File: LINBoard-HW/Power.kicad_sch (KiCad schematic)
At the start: 18 parts, among them U3 TPS56339DDC, U4 LD1117S33CTR

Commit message: board layout started
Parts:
- C24, C25, C26, C27, C28, C29, C30, C31: footprint Capacitor_SMD:C_0603_1608Metric -> Capacitor_SMD:C_0402_1005Metric
- D3: value SCHOTTKY -> Schottky; footprint (none) -> Diode_SMD:D_SOD-123
- D6: footprint LED_SMD:LED_0805_2012Metric -> LED_SMD:LED_0603_1608Metric
- L2: footprint (none) -> Inductors_SMD:Wuerth_LHMI
- R21, R22, R23, R24: footprint Resistor_SMD:R_0603_1608Metric -> Resistor_SMD:R_0402_1005Metric
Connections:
- net SW: now reaches C27.2, L2.1, U3.2 (SW)
- net +12P: now reaches C24.1, C25.1, C26.1, D3.1 (K), U3.3 (VIN)
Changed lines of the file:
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@@
+	)
+	(junction
+		(at 35.56 31.75)
+		(diameter 0)
+		(color 0 0 0 0)
 	)
 	(junction
@@
 	(wire
 		(pts
+			(xy 35.56 29.21) (xy 35.56 31.75)
+		)
+		(stroke
+			(width 0)
+			(type default)
+		)
+	)
+	(wire
+		(pts
 			(xy 200.66 45.72) (xy 200.66 48.26)
 		)
@@
 			(width 0)
 			(type default)
+		)
+	)
+	(label "SW"
+		(at 96.52 34.29 0)
+		(effects
+			(font
+				(size 1.27 1.27)
+				(thickness 0.254)
+				(bold yes)
+			)
+			(justify left bottom)
 		)
 	)
@@
 			)
 		)
-		(property "Footprint" "Resistor_SMD:R_0603_1608Metric"
+		(property "Footprint" "Resistor_SMD:R_0402_1005Metric"
 			(at 200.66 43.18 0)
 			(effects
@@
 			)
 		)
-		(property "Footprint" "Resistor_SMD:R_0603_1608Metric"
+		(property "Footprint" "Resistor_SMD:R_0402_1005Metric"
 			(at 95.25 43.18 0)
 			(effects
@@
 			)
 		)
-		(property "Footprint" ""
+		(property "Footprint" "Inductors_SMD:Wuerth_LHMI"
 			(at 113.03 34.29 0)
 			(effects
@@
 			)
 		)
-		(property "Footprint" "Capacitor_SMD:C_0603_1608Metric"
+		(property "Footprint" "Capacitor_SMD:C_0402_1005Metric"
 			(at 55.88 44.45 0)
 			(effects
@@
 			)
 		)
-		(property "Footprint" "Resistor_SMD:R_0603_1608Metric"
+		(property "Footprint" "Resistor_SMD:R_0402_1005Metric"
 			(at 119.38 44.45 0)
 			(effects
@@
 			)
 		)
-		(property "Footprint" "Capacitor_SMD:C_0603_1608Metric"
+		(property "Footprint" "Capacitor_SMD:C_0402_1005Metric"
 			(at 101.6 43.18 0)
 			(effects
@@
 			)
 		)
-		(property "Footprint" "Capacitor_SMD:C_0603_1608Metric"
+		(property "Footprint" "Capacitor_SMD:C_0402_1005Metric"
 			(at 132.08 39.37 0)
 			(effects
@@
 			)
 		)
-		(property "Footprint" "Resistor_SMD:R_0603_1608Metric"
+		(property "Footprint" "Resistor_SMD:R_0402_1005Metric"
 			(at 119.38 54.61 0)
 			(effects
@@
 			)
 		)
-		(property "Footprint" "Capacitor_SMD:C_0603_1608Metric"
+		(property "Footprint" "Capacitor_SMD:C_0402_1005Metric"
 			(at 35.56 44.45 0)
 			(effects
@@
 			)
 		)
-		(property "Footprint" "Capacitor_SMD:C_0603_1608Metric"
+		(property "Footprint" "Capacitor_SMD:C_0402_1005Metric"
 			(at 187.96 39.37 0)
 			(effects
@@
 			)
 		)
-		(property "Footprint" "LED_SMD:LED_0805_2012Metric"
+		(property "Footprint" "LED_SMD:LED_0603_1608Metric"
 			(at 200.66 50.8 90)
 			(effects
@@
 			)
 		)
-		(property "Footprint" "Capacitor_SMD:C_0603_1608Metric"
+		(property "Footprint" "Capacitor_SMD:C_0402_1005Metric"
 			(at 45.72 44.45 0)
 			(effects
@@
 			)
 		)
-		(property "Footprint" "Capacitor_SMD:C_0603_1608Metric"
+		(property "Footprint" "Capacitor_SMD:C_0402_1005Metric"
 			(at 157.48 39.37 0)
 			(effects
@@
 	)
 	(symbol
+		(lib_id "power:+12P")
+		(at 35.56 29.21 0)
+		(unit 1)
+		(exclude_from_sim no)
+		(in_bom yes)
+		(on_board yes)
+		(dnp no)
+		(fields_autoplaced yes)
+		(property "Reference" "#PWR045"
+			(at 35.56 33.02 0)
+			(effects
+				(font
+					(size 1.27 1.27)
+				)
+				(hide yes)
+			)
+		)
+		(property "Value" "+12P"
+			(at 35.56 24.13 0)
+			(effects
+				(font
+					(size 1.27 1.27)
+				)
+			)
+		)
+		(property "Footprint" ""
+			(at 35.56 29.21 0)
+			(effects
+				(font
+					(size 1.27 1.27)
+				)
+				(hide yes)
+			)
+		)
+		(property "Datasheet" ""
+			(at 35.56 29.21 0)
+			(effects
+				(font
+					(size 1.27 1.27)
+				)
+				(hide yes)
+			)
+		)
+		(property "Description" "Power symbol creates a global label with name \"+12P\""
+			(at 35.56 29.21 0)
+			(effects
+				(font
+					(size 1.27 1.27)
+				)
+				(hide yes)
+			)
+		)
+		(pin "1"
+		)
+		(instances
+			(project ""
+				(path "/27863e5d-8a22-474c-850d-36d8970b0f4a/f2430bd2-0c34-49e2-a275-9ffcb384aba8"
+					(reference "#PWR045")
+					(unit 1)
+				)
+			)
+		)
+	)
+	(symbol
 		(lib_id "Jumper:Jumper_2_Small_Bridged")
 		(at 200.66 38.1 90)
@@
 			)
 		)
-		(property "Footprint" "Capacitor_SMD:C_0603_1608Metric"
+		(property "Footprint" "Capacitor_SMD:C_0402_1005Metric"
 			(at 142.24 39.37 0)
 			(effects
@@
 			)
 		)
-		(property "Value" "SCHOTTKY"
+		(property "Value" "Schottky"
 			(at 28.194 37.592 0)
 			(effects
@@
 			)
 		)
-		(property "Footprint" ""
+		(property "Footprint" "Diode_SMD:D_SOD-123"
 			(at 27.94 31.75 90)
 			(effects

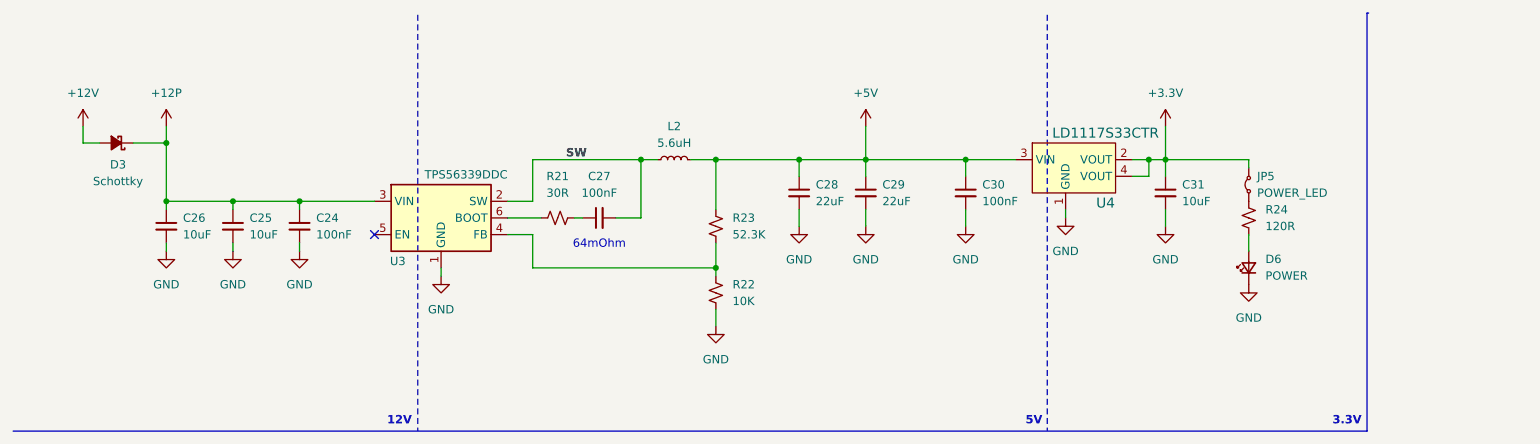
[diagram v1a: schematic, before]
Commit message: change usb
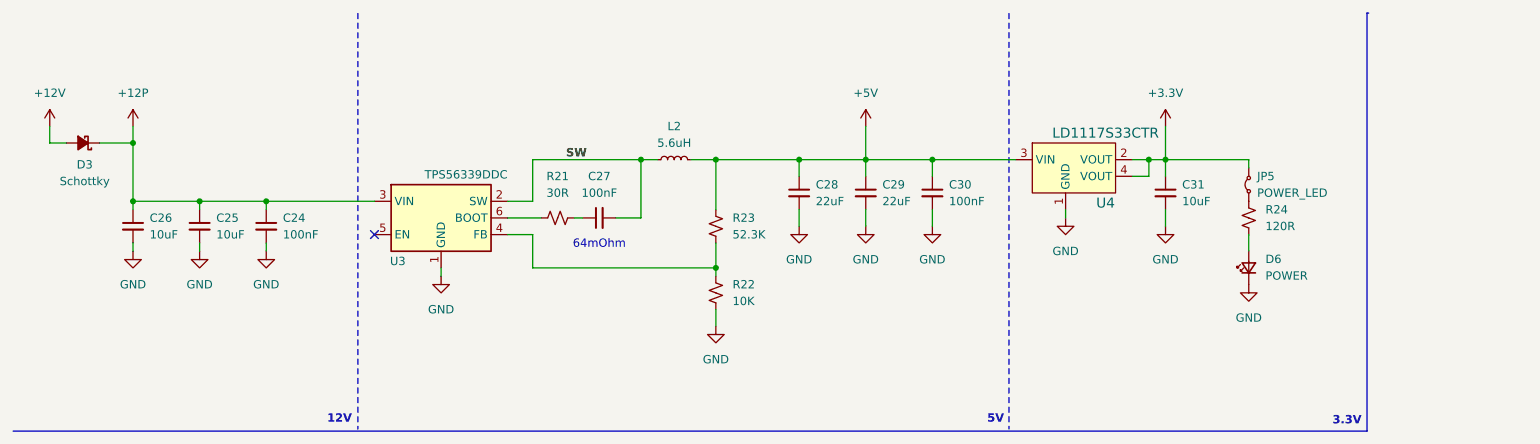
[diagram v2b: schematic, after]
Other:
- moved on the sheet: C24, C25, C26, C30, D3

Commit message: doing some layout
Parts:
- C24, C25, C26, C27, C28, C29, C30, C31: footprint Capacitor_SMD:C_0402_1005Metric -> Capacitor_SMD:C_0805_2012Metric
- D6: footprint LED_SMD:LED_0603_1608Metric -> LED_SMD:LED_0805_2012Metric
- R21, R22, R23, R24: footprint Resistor_SMD:R_0402_1005Metric -> Resistor_SMD:R_0805_2012Metric
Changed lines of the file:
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@@
 			)
 		)
-		(property "Footprint" "Resistor_SMD:R_0402_1005Metric"
+		(property "Footprint" "Resistor_SMD:R_0805_2012Metric"
 			(at 200.66 43.18 0)
 			(effects
@@
 			)
 		)
-		(property "Footprint" "Resistor_SMD:R_0402_1005Metric"
+		(property "Footprint" "Resistor_SMD:R_0805_2012Metric"
 			(at 95.25 43.18 0)
 			(effects
@@
 			)
 		)
-		(property "Footprint" "Capacitor_SMD:C_0402_1005Metric"
+		(property "Footprint" "Capacitor_SMD:C_0805_2012Metric"
 			(at 50.8 44.45 0)
 			(effects
@@
 			)
 		)
-		(property "Footprint" "Resistor_SMD:R_0402_1005Metric"
+		(property "Footprint" "Resistor_SMD:R_0805_2012Metric"
 			(at 119.38 44.45 0)
 			(effects
@@
 			)
 		)
-		(property "Footprint" "Capacitor_SMD:C_0402_1005Metric"
+		(property "Footprint" "Capacitor_SMD:C_0805_2012Metric"
 			(at 101.6 43.18 0)
 			(effects
@@
 			)
 		)
-		(property "Footprint" "Capacitor_SMD:C_0402_1005Metric"
+		(property "Footprint" "Capacitor_SMD:C_0805_2012Metric"
 			(at 132.08 39.37 0)
 			(effects
@@
 			)
 		)
-		(property "Footprint" "Resistor_SMD:R_0402_1005Metric"
+		(property "Footprint" "Resistor_SMD:R_0805_2012Metric"
 			(at 119.38 54.61 0)
 			(effects
@@
 			)
 		)
-		(property "Footprint" "Capacitor_SMD:C_0402_1005Metric"
+		(property "Footprint" "Capacitor_SMD:C_0805_2012Metric"
 			(at 30.48 44.45 0)
 			(effects
@@
 			)
 		)
-		(property "Footprint" "Capacitor_SMD:C_0402_1005Metric"
+		(property "Footprint" "Capacitor_SMD:C_0805_2012Metric"
 			(at 187.96 39.37 0)
 			(effects
@@
 			)
 		)
-		(property "Footprint" "LED_SMD:LED_0603_1608Metric"
+		(property "Footprint" "LED_SMD:LED_0805_2012Metric"
 			(at 200.66 50.8 90)
 			(effects
@@
 			)
 		)
-		(property "Footprint" "Capacitor_SMD:C_0402_1005Metric"
+		(property "Footprint" "Capacitor_SMD:C_0805_2012Metric"
 			(at 40.64 44.45 0)
 			(effects
@@
 			)
 		)
-		(property "Footprint" "Capacitor_SMD:C_0402_1005Metric"
+		(property "Footprint" "Capacitor_SMD:C_0805_2012Metric"
 			(at 152.4 39.37 0)
 			(effects
@@
 			)
 		)
-		(property "Footprint" "Capacitor_SMD:C_0402_1005Metric"
+		(property "Footprint" "Capacitor_SMD:C_0805_2012Metric"
 			(at 142.24 39.37 0)
 			(effects

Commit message: routing first pass complete
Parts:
- removed D3: Schottky, Diode_SMD:D_SOD-123, symbol Device:D_Schottky_Small_Filled
- added D9: Schottky, Diode_SMD:D_SOD-123, symbol Device:D_Schottky_Small_Filled
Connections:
- net +12P: now also D9.1 (K)
- net +12V: now also D9.2 (A)
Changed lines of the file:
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@@
+	)
+	(junction
+		(at 30.48 22.86)
+		(diameter 0)
+		(color 0 0 0 0)
 	)
 	(junction
@@
 	)
 	(junction
-		(at 30.48 31.75)
-		(diameter 0)
-		(color 0 0 0 0)
-	)
-	(junction
 		(at 50.8 40.64)
 		(diameter 0)
@@
 	(wire
 		(pts
-			(xy 30.48 29.21) (xy 30.48 31.75)
+			(xy 30.48 20.32) (xy 30.48 22.86)
 		)
 		(stroke
@@
 	(wire
 		(pts
-			(xy 25.4 31.75) (xy 30.48 31.75)
-		)
-		(stroke
-			(width 0)
-			(type default)
-		)
-	)
-	(wire
-		(pts
 			(xy 50.8 48.26) (xy 50.8 46.99)
 		)
@@
 	(wire
 		(pts
-			(xy 17.78 29.21) (xy 17.78 31.75)
-		)
-		(stroke
-			(width 0)
-			(type default)
-		)
-	)
-	(wire
-		(pts
-			(xy 17.78 31.75) (xy 20.32 31.75)
+			(xy 17.78 20.32) (xy 17.78 22.86)
 		)
 		(stroke
@@
 	(wire
 		(pts
-			(xy 30.48 31.75) (xy 30.48 40.64)
-		)
-		(stroke
-			(width 0)
-			(type default)
-		)
-	)
-	(wire
-		(pts
 			(xy 119.38 57.15) (xy 119.38 59.69)
 		)
@@
 	(wire
 		(pts
+			(xy 17.78 22.86) (xy 20.32 22.86)
+		)
+		(stroke
+			(width 0)
+			(type default)
+		)
+	)
+	(wire
+		(pts
 			(xy 91.44 40.64) (xy 91.44 34.29)
 		)
@@
 	(wire
 		(pts
+			(xy 30.48 22.86) (xy 30.48 40.64)
+		)
+		(stroke
+			(width 0)
+			(type default)
+		)
+	)
+	(wire
+		(pts
 			(xy 185.42 36.83) (xy 185.42 34.29)
 		)
@@
 		(pts
 			(xy 152.4 34.29) (xy 152.4 36.83)
+		)
+		(stroke
+			(width 0)
+			(type default)
+		)
+	)
+	(wire
+		(pts
+			(xy 25.4 22.86) (xy 30.48 22.86)
 		)
 		(stroke
@@
 	)
 	(symbol
+		(lib_id "Device:D_Schottky_Small_Filled")
+		(at 22.86 22.86 180)
+		(unit 1)
+		(exclude_from_sim no)
+		(in_bom yes)
+		(on_board yes)
+		(dnp no)
+		(property "Reference" "D9"
+			(at 23.114 26.162 0)
+			(effects
+				(font
+					(size 1.27 1.27)
+				)
+			)
+		)
+		(property "Value" "Schottky"
+			(at 23.114 28.702 0)
+			(effects
+				(font
+					(size 1.27 1.27)
+				)
+			)
+		)
+		(property "Footprint" "Diode_SMD:D_SOD-123"
+			(at 22.86 22.86 90)
+			(effects
+				(font
+					(size 1.27 1.27)
+				)
+				(hide yes)
+			)
+		)
+		(property "Datasheet" "~"
+			(at 22.86 22.86 90)
+			(effects
+				(font
+					(size 1.27 1.27)
+				)
+				(hide yes)
+			)
+		)
+		(property "Description" "Schottky diode, small symbol, filled shape"
+			(at 22.86 22.86 0)
+			(effects
+				(font
+					(size 1.27 1.27)
+				)
+				(hide yes)
+			)
+		)
+		(pin "1"
+		)
+		(pin "2"
+		)
+		(instances
+			(project "LINBoard-HW"
+				(path "/27863e5d-8a22-474c-850d-36d8970b0f4a/f2430bd2-0c34-49e2-a275-9ffcb384aba8"
+					(reference "D9")
+					(unit 1)
+				)
+			)
+		)
+	)
+	(symbol
 		(lib_id "power:GND")
 		(at 187.96 44.45 0)
@@
 	(symbol
 		(lib_id "power:+12V")
-		(at 17.78 29.21 0)
+		(at 17.78 20.32 0)
 		(unit 1)
 		(exclude_from_sim no)
@@
 		(fields_autoplaced yes)
 		(property "Reference" "#PWR07"
-			(at 17.78 33.02 0)
+			(at 17.78 24.13 0)
 			(effects
 				(font
@@
 		)
 		(property "Value" "+12V"
-			(at 17.78 24.13 0)
+			(at 17.78 15.24 0)
 			(effects
 				(font
@@
 		)
 		(property "Footprint" ""
-			(at 17.78 29.21 0)
+			(at 17.78 20.32 0)
 			(effects
 				(font
@@
 		)
 		(property "Datasheet" ""
-			(at 17.78 29.21 0)
+			(at 17.78 20.32 0)
 			(effects
 				(font
@@
 		)
 		(property "Description" "Power symbol creates a global label with name \"+12V\""
-			(at 17.78 29.21 0)
+			(at 17.78 20.32 0)
 			(effects
 				(font
@@
 	(symbol
 		(lib_id "power:+12P")
-		(at 30.48 29.21 0)
+		(at 30.48 20.32 0)
 		(unit 1)
 		(exclude_from_sim no)
@@
 		(fields_autoplaced yes)
 		(property "Reference" "#PWR045"
-			(at 30.48 33.02 0)
+			(at 30.48 24.13 0)
 			(effects
 				(font
@@
 		)
 		(property "Value" "+12P"
-			(at 30.48 24.13 0)
+			(at 30.48 15.24 0)
 			(effects
 				(font
@@
 		)
 		(property "Footprint" ""
-			(at 30.48 29.21 0)
+			(at 30.48 20.32 0)
 			(effects
 				(font
@@
 		)
 		(property "Datasheet" ""
-			(at 30.48 29.21 0)
+			(at 30.48 20.32 0)
 			(effects
 				(font
@@
 		)
 		(property "Description" "Power symbol creates a global label with name \"+12P\""
-			(at 30.48 29.21 0)
+			(at 30.48 20.32 0)
 			(effects
 				(font
@@
 					(unit 1)
 				)
-			)
-		)
-	)
-	(symbol
-		(lib_id "Device:D_Schottky_Small_Filled")
-		(at 22.86 31.75 180)
-		(unit 1)
-		(exclude_from_sim no)
-		(in_bom yes)
-		(on_board yes)
-		(dnp no)
-		(property "Reference" "D3"
-			(at 23.114 35.052 0)
-			(effects
-				(font
-					(size 1.27 1.27)
-				)
-			)
-		)
-		(property "Value" "Schottky"
-			(at 23.114 37.592 0)
-			(effects
-				(font
-					(size 1.27 1.27)
-				)
-			)
-		)
-		(property "Footprint" "Diode_SMD:D_SOD-123"
-			(at 22.86 31.75 90)
-			(effects
-				(font
-					(size 1.27 1.27)
-				)
-				(hide yes)
-			)
-		)
-		(property "Datasheet" "~"
-			(at 22.86 31.75 90)
-			(effects
-				(font
-					(size 1.27 1.27)
-				)
-				(hide yes)
-			)
-		)
-		(property "Description" "Schottky diode, small symbol, filled shape"
-			(at 22.86 31.75 0)
-			(effects
-				(font
-					(size 1.27 1.27)
-				)
-				(hide yes)
-			)
-		)
-		(pin "1"
-		)
-		(pin "2"
-		)
-		(instances
-			(project "LINBoard-HW"
-				(path "/27863e5d-8a22-474c-850d-36d8970b0f4a/f2430bd2-0c34-49e2-a275-9ffcb384aba8"
-					(reference "D3")
-					(unit 1)
-				)

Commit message: add fab outputs
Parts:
- C24, C27, C30: LCSC Part (none) -> C49678
- C25, C26, C31: LCSC Part (none) -> C15850
- C28, C29: LCSC Part (none) -> C45783
- D6: LCSC Part (none) -> C2297
- D9: LCSC Part (none) -> C179426
- JP5: now left out of the parts list
- L2: LCSC Part (none) -> C467062
- R21: LCSC Part (none) -> C325808
- R22: LCSC Part (none) -> C17414
- R23: LCSC Part (none) -> C17740
- R24: LCSC Part (none) -> C229076
- U3: LCSC Part (none) -> C2071106
- U4: LCSC Part (none) -> C35879
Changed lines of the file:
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@@
+			)
+		)
+		(property "LCSC Part" "C229076"
+			(at 200.66 43.18 0)
+			(effects
+				(font
+					(size 1.27 1.27)
+				)
+				(hide yes)
 			)
 		)
@@
 			)
 		)
+		(property "LCSC Part" "C325808"
+			(at 95.25 43.18 90)
+			(effects
+				(font
+					(size 1.27 1.27)
+				)
+				(hide yes)
+			)
+		)
 		(pin "1"
 		)
@@
 			)
 		)
+		(property "LCSC Part" "C467062"
+			(at 113.03 34.29 90)
+			(effects
+				(font
+					(size 1.27 1.27)
+				)
+				(hide yes)
+			)
+		)
 		(pin "1"
 		)
@@
 			)
 		)
+		(property "LCSC Part" "C49678"
+			(at 50.8 44.45 0)
+			(effects
+				(font
+					(size 1.27 1.27)
+				)
+				(hide yes)
+			)
+		)
 		(pin "1"
 		)
@@
 			)
 		)
+		(property "LCSC Part" "C17740"
+			(at 119.38 44.45 0)
+			(effects
+				(font
+					(size 1.27 1.27)
+				)
+				(hide yes)
+			)
+		)
 		(pin "1"
 		)
@@
 			)
 		)
+		(property "LCSC Part" "C49678"
+			(at 101.6 43.18 90)
+			(effects
+				(font
+					(size 1.27 1.27)
+				)
+				(hide yes)
+			)
+		)
 		(pin "1"
 		)
@@
 			)
 		)
+		(property "LCSC Part" "C45783"
+			(at 132.08 39.37 0)
+			(effects
+				(font
+					(size 1.27 1.27)
+				)
+				(hide yes)
+			)
+		)
 		(pin "1"
 		)
@@
 			)
 		)
+		(property "LCSC Part" "C179426"
+			(at 22.86 22.86 0)
+			(effects
+				(font
+					(size 1.27 1.27)
+				)
+				(hide yes)
+			)
+		)
 		(pin "1"
 		)
@@
 			)
 		)
+		(property "LCSC Part" "C17414"
+			(at 119.38 54.61 0)
+			(effects
+				(font
+					(size 1.27 1.27)
+				)
+				(hide yes)
+			)
+		)
 		(pin "1"
 		)
@@
 			)
 		)
+		(property "LCSC Part" "C15850"
+			(at 30.48 44.45 0)
+			(effects
+				(font
+					(size 1.27 1.27)
+				)
+				(hide yes)
+			)
+		)
 		(pin "1"
 		)
@@
 			)
 		)
+		(property "LCSC Part" "C15850"
+			(at 187.96 39.37 0)
+			(effects
+				(font
+					(size 1.27 1.27)
+				)
+				(hide yes)
+			)
+		)
 		(pin "1"
 		)
@@
 			)
 		)
+		(property "LCSC Part" "C2297"
+			(at 200.66 50.8 90)
+			(effects
+				(font
+					(size 1.27 1.27)
+				)
+				(hide yes)
+			)
+		)
 		(pin "2"
 		)
@@
 			)
 		)
+		(property "LCSC Part" "C15850"
+			(at 40.64 44.45 0)
+			(effects
+				(font
+					(size 1.27 1.27)
+				)
+				(hide yes)
+			)
+		)
 		(pin "1"
 		)
@@
 			)
 		)
+		(property "LCSC Part" "C49678"
+			(at 152.4 39.37 0)
+			(effects
+				(font
+					(size 1.27 1.27)
+				)
+				(hide yes)
+			)
+		)
 		(pin "1"
 		)
@@
 			)
 		)
+		(property "LCSC Part" "C35879"
+			(at 172.72 34.29 0)
+			(effects
+				(font
+					(size 1.27 1.27)
+				)
+				(hide yes)
+			)
+		)
 		(pin "1"
 		)
@@
 			)
 		)
+		(property "LCSC Part" "C2071106"
+			(at 77.47 43.18 0)
+			(effects
+				(font
+					(size 1.27 1.27)
+				)
+				(hide yes)
+			)
+		)
 		(pin "5"
 		)
@@
 		(unit 1)
 		(exclude_from_sim no)
-		(in_bom yes)
+		(in_bom no)
 		(on_board yes)
 		(dnp no)
@@
 			)
 		)
+		(property "LCSC Part" ""
+			(at 200.66 38.1 90)
+			(effects
+				(font
+					(size 1.27 1.27)
+				)
+				(hide yes)
+			)
+		)
 		(pin "1"
 		)
@@
 			(at 142.24 39.37 0)
 			(effects
+				(font
+					(size 1.27 1.27)
+				)
+				(hide yes)
+			)
+		)
+		(property "LCSC Part" "C45783"
+			(at 142.24 39.37 0)
+			(effects

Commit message: change pinout, export
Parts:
- R24: LCSC Part C229076 -> C17437
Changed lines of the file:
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@@
 			)
 		)
-		(property "LCSC Part" "C229076"
+		(property "LCSC Part" "C17437"
 			(at 200.66 43.18 0)
 			(effects

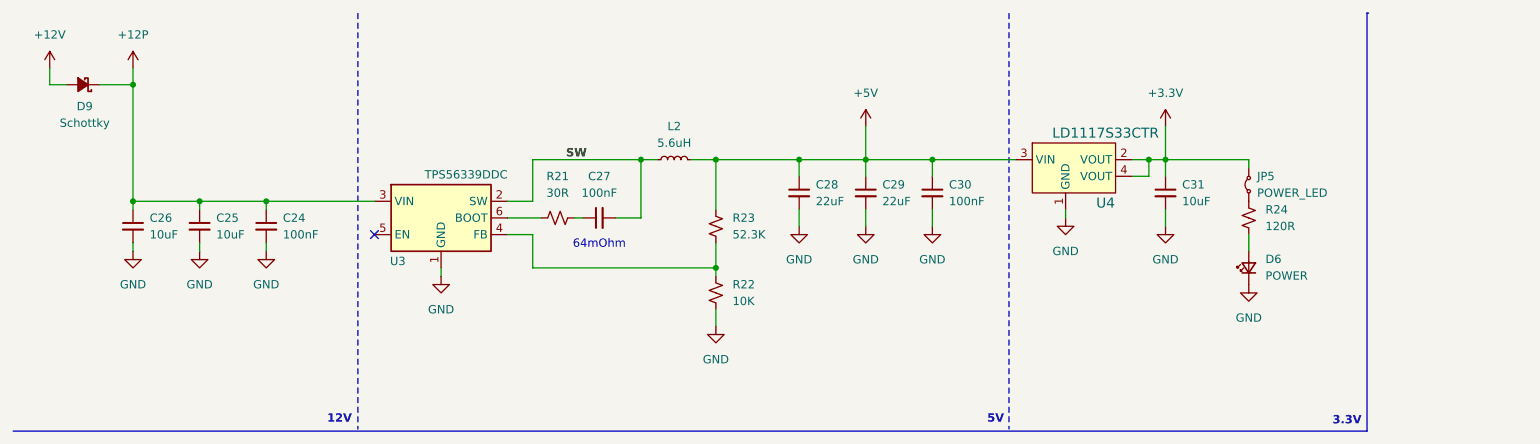
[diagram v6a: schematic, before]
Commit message: add tvs, fix reset button
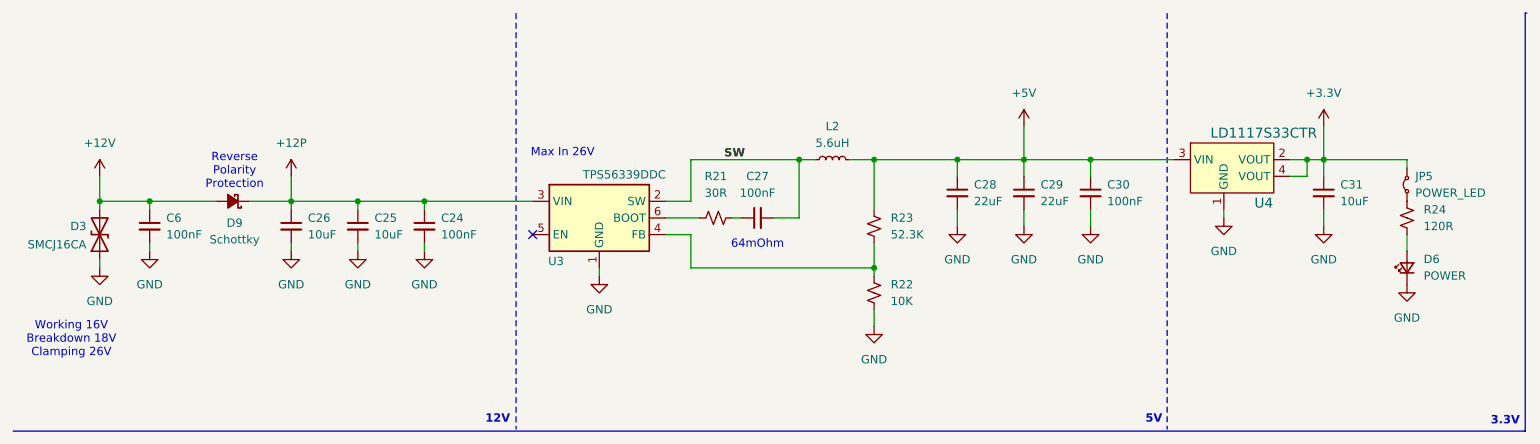
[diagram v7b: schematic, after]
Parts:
- added C6: 100nF, Capacitor_SMD:C_0805_2012Metric, symbol Device:C_Small
- added D3: SMCJ16CA, digikey-footprints:DO-214AB_TVS, symbol Device:D_TVS
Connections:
- net +12V: now also C6.1, D3.2 (A2)
- net GND: now also C6.2, D3.1 (A1)
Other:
- note added: "Max In 26V"
- note added: "Reverse Polarity Protection"
- note added: "Working 16V Breakdown 18V Clamping 26V"
- moved on the sheet: C24, C25, C26, C27, C28, C29, C30, C31, D6, D9, JP5, L2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
